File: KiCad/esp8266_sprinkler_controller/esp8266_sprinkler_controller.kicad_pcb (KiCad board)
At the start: 2 copper layers, 73.2 x 80.3 mm, 27 parts, among them J1 Barrel_Jack_Switch, J2 Screw_Terminal_01x02 ST1, J3 Screw_Terminal_01x02 ST2, J4 Screw_Terminal_01x02 ST3, J5 Screw_Terminal_01x02 ST4, SW1 SW_Push, U1 LM7805_TO220, U2 WeMos_D1_mini, U3 74HC595, U4 L293D, U5 L293D

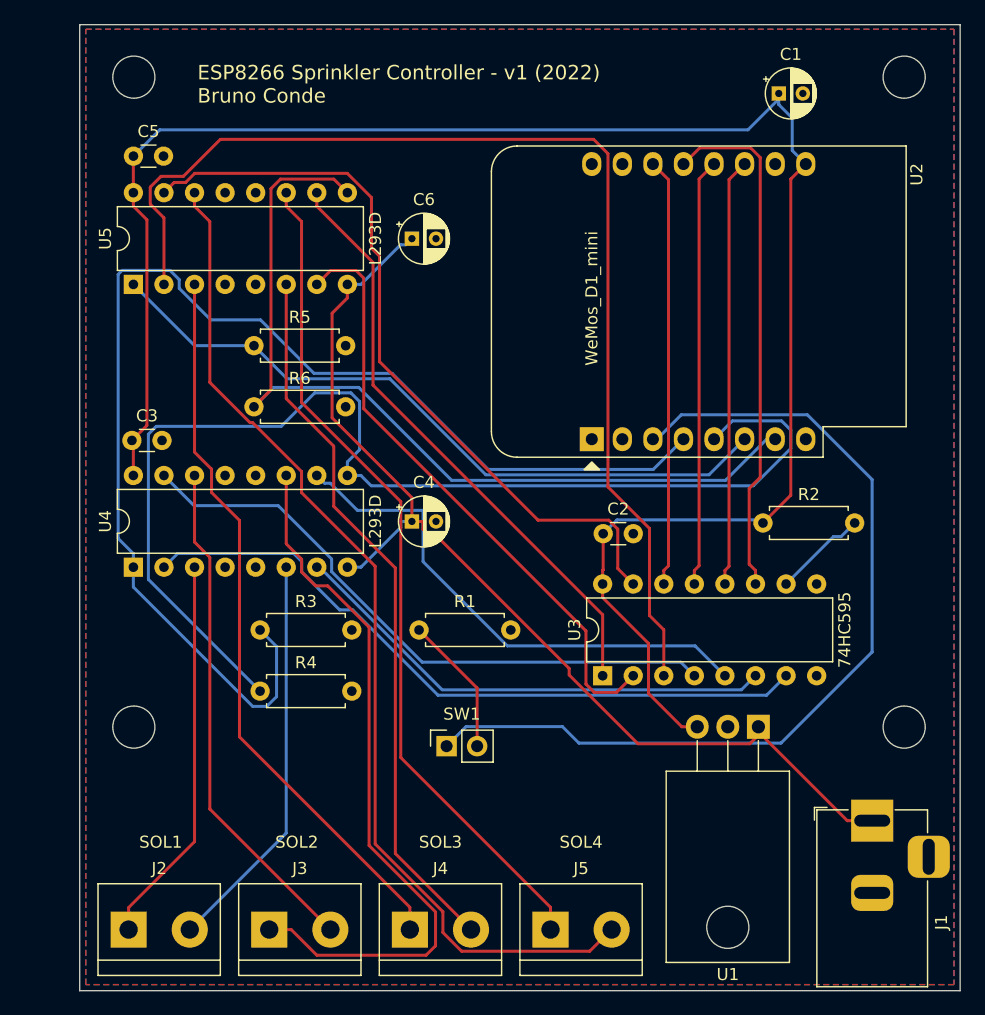
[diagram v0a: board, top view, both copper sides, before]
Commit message: Researching a way to use less power when the circuit is in deep sleep; Updated Kicad schematic and pcb design
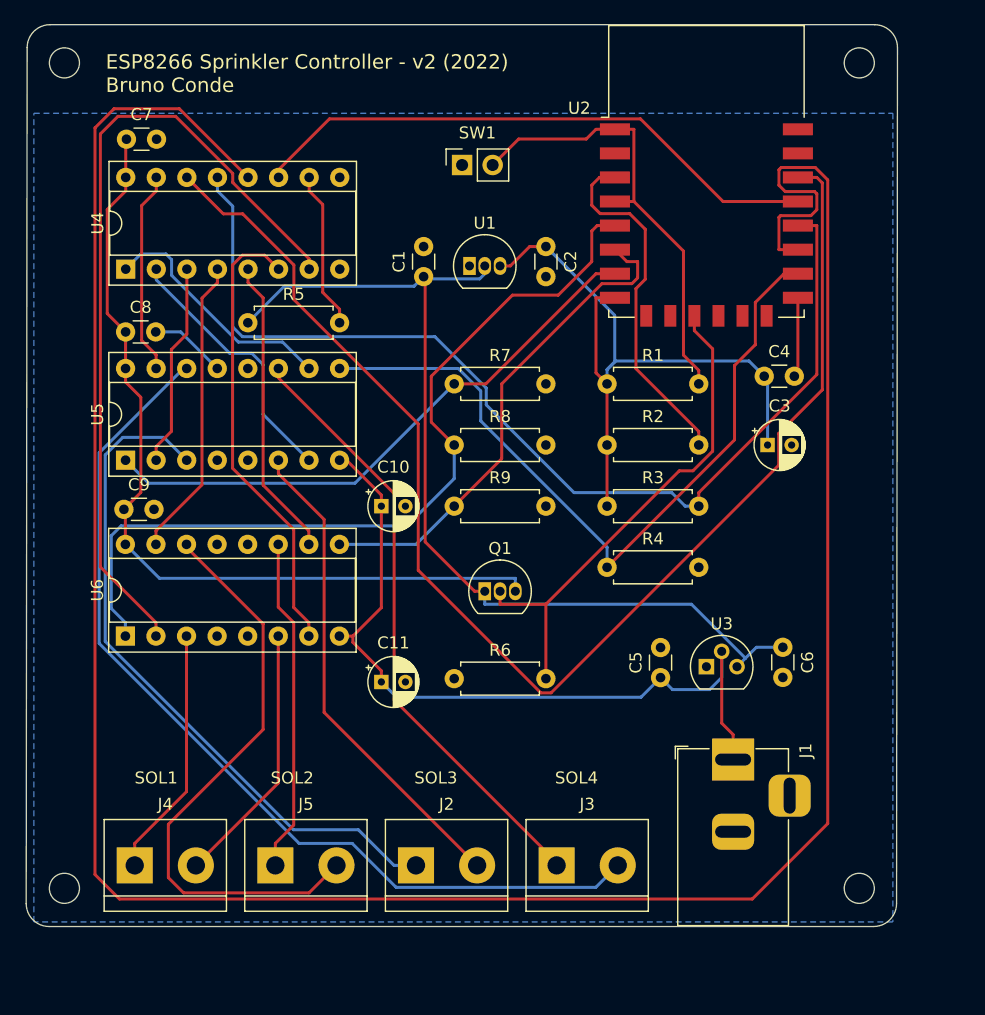
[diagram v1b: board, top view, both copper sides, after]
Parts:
- removed the R5 at (78.0, 67.3)
- removed REF** (x4): MountingHole_3.5mm, MountingHole:MountingHole_3.5mm
- added C10: C_Polarized_Small, Capacitor_THT:CP_Radial_D4.0mm_P2.00mm, F.Cu at (88.6, 80.6)
- added C2: C_Small, Capacitor_THT:C_Disc_D3.0mm_W1.6mm_P2.50mm, F.Cu at (102.2, 59.1)
- added C3: C_Polarized, Capacitor_THT:CP_Radial_D4.0mm_P2.00mm, F.Cu at (120.7, 75.6)
- added C4: C_Small, Capacitor_THT:C_Disc_D3.0mm_W1.6mm_P2.50mm, F.Cu at (120.4, 69.8)
- added C5: C_Small, Capacitor_THT:C_Disc_D3.0mm_W1.6mm_P2.50mm, F.Cu at (111.8, 94.9)
- added Q1: BC547, Package_TO_SOT_THT:TO-92_Inline, F.Cu at (97.2, 87.7)
- added R2: 10KΩ, Resistor_THT:R_Axial_DIN0207_L6.3mm_D2.5mm_P7.62mm_Horizontal, F.Cu at (107.3, 75.6)
- added R7: 1KΩ, Resistor_THT:R_Axial_DIN0207_L6.3mm_D2.5mm_P7.62mm_Horizontal, F.Cu at (94.6, 70.5)
- added R8: 1KΩ, Resistor_THT:R_Axial_DIN0207_L6.3mm_D2.5mm_P7.62mm_Horizontal, F.Cu at (94.6, 75.6)
- added R9: 1KΩ, Resistor_THT:R_Axial_DIN0207_L6.3mm_D2.5mm_P7.62mm_Horizontal, F.Cu at (94.6, 80.6)
- added REF1: MountingHole_2.5mm, MountingHole:MountingHole_2.5mm, F.Cu at (62.2, 112.4)
- added REF2: MountingHole_2.5mm, MountingHole:MountingHole_2.5mm, F.Cu at (128.3, 112.4)
- added REF3: MountingHole_2.5mm, MountingHole:MountingHole_2.5mm, F.Cu at (62.2, 43.8)
- added REF4: MountingHole_2.5mm, MountingHole:MountingHole_2.5mm, F.Cu at (128.3, 43.8)
- added U3: MCP1700-5002E_TO92, Package_TO_SOT_THT:TO-92, F.Cu at (115.6, 94.0)
- C1: value C_Polarized -> C_Small; footprint Capacitor_THT:CP_Radial_D4.0mm_P2.00mm -> Capacitor_THT:C_Disc_D3.0mm_W1.6mm_P2.50mm
- C6: value C_Polarized_Small -> C_Small; footprint Capacitor_THT:CP_Radial_D4.0mm_P2.00mm -> Capacitor_THT:C_Disc_D3.0mm_W1.6mm_P2.50mm
- R3, R4: value 1KΩ -> 10KΩ
- U1: value LM7805_TO220 -> MCP1700-3002E_TO92; footprint Package_TO_SOT_THT:TO-220-3_Horizontal_TabDown -> Package_TO_SOT_THT:TO-92_Inline
- U2: value WeMos_D1_mini -> ESP-12F; footprint Module:WEMOS_D1_mini_light -> RF_Module:ESP-12E
- U4: renamed from U3; footprint Package_DIP:DIP-16_W7.62mm -> Package_DIP:DIP-16_W7.62mm_Socket
- U5: footprint Package_DIP:DIP-16_W7.62mm -> Package_DIP:DIP-16_W7.62mm_Socket
- U6: renamed from U4; footprint Package_DIP:DIP-16_W7.62mm -> Package_DIP:DIP-16_W7.62mm_Socket
- moved U4 52.1 mm to (67.3, 61.0)
- moved C7 51.4 mm to (67.4, 50.2)
- moved SW1 48.3 mm to (95.3, 52.3)
- moved R5 45.9 mm to (77.5, 65.4)
- moved C6 45.9 mm to (121.9, 92.4), turned to -90 degrees
- moved U1 45.2 mm to (95.9, 60.7), turned to 0 degrees
- moved C1 33.2 mm to (92.1, 61.6), turned to 90 degrees
- moved R3 30.6 mm to (107.3, 80.6)
- moved R4 30.6 mm to (107.3, 85.7)
- moved R6 28.1 mm to (94.6, 95.0)
- moved R1 25.7 mm to (107.3, 70.5)
- moved U2 24.2 mm to (115.6, 52.8), turned to 0 degrees
- moved C8 14.6 mm to (67.3, 66.2)
- moved U5 14.6 mm to (67.3, 76.8)
- moved C11 13.6 mm to (88.6, 95.2)
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- renumbered C4 to C11, C2 to C7, C5 to C8, C3 to C9, J4 to J2, J5 to J3, J2 to J4, J3 to J5, R2 to R5
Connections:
- net Net-(U3-Pad1) renamed /QB
- net Net-(U3-Pad15) renamed /QA
- net Net-(U3-Pad2) renamed /QC
- net Net-(U3-Pad3) renamed /QD
- net Net-(U3-Pad4) renamed /QE
- net Net-(U3-Pad5) renamed /QF
- net Net-(U3-Pad6) renamed /QG
- net Net-(U3-Pad7) renamed /QH
- C6 pad 1: +9V -> +5V
- C7 pad 1: +5V -> /+5V_EN
- C8 pad 1: +5V -> /+5V_EN
- C9 pad 1: +5V -> /+5V_EN
- R1 pad 1: Net-(R1-Pad1) -> +3V3
- R1 pad 2: GND -> Net-(R1-Pad2)
- R3 pad 1: Net-(R3-Pad1) -> +3V3
- R3 pad 2: GND -> /GPIO0
- R4 pad 1: Net-(R4-Pad1) -> /GPIO15
- R6 pad 1: Net-(R6-Pad1) -> GND
- R6 pad 2: GND -> /GPIO9
- SW1 pad 1: Net-(SW1-Pad1) -> GND
- SW1 pad 2: Net-(R1-Pad1) -> Net-(R1-Pad2)
- U1 pad 1: +9V -> GND
- U1 pad 2: GND -> +5V
- U1 pad 3: +5V -> +3V3
- U2 pad 1: unconnected-(U2-Pad1) -> Net-(R1-Pad2)
- U2 pad 10: GND -> unconnected-(U2-Pad10)
- U2 pad 11: Net-(U2-Pad11) -> /GPIO9
- U2 pad 12: Net-(U2-Pad12) -> unconnected-(U2-Pad12)
- U2 pad 13: Net-(U2-Pad13) -> unconnected-(U2-Pad13)
- U2 pad 14: Net-(U2-Pad14) -> unconnected-(U2-Pad14)
- U2 pad 15: unconnected-(U2-Pad15) -> GND
- U2 pad 16: unconnected-(U2-Pad16) -> /GPIO15
- U2 pad 3: Net-(SW1-Pad1) -> Net-(R2-Pad2)
- U2 pad 4: Net-(R3-Pad1) -> Net-(R1-Pad2)
- U2 pad 5: Net-(R4-Pad1) -> /GPIO14
- U2 pad 6: Net-(R5-Pad1) -> /GPIO12
- U2 pad 7: Net-(R6-Pad1) -> /GPIO13
- U2 pad 8: unconnected-(U2-Pad8) -> +3V3
- U2 pad 9: +5V -> unconnected-(U2-Pad9)
- U4 pad 11: Net-(U2-Pad13) -> /GPIO4
- U4 pad 12: Net-(U2-Pad11) -> /GPIO2
- U4 pad 13: Net-(U2-Pad12) -> /GPIO0
- U4 pad 14: Net-(U2-Pad14) -> /GPIO5
- U4 pad 16: +5V -> /+5V_EN
- U5 pad 1: Net-(R5-Pad1) -> /GPIO13
- U5 pad 16: +5V -> /+5V_EN
- U5 pad 9: Net-(R6-Pad1) -> /GPIO15
- U6 pad 1: Net-(R3-Pad1) -> /GPIO14
- U6 pad 16: +5V -> /+5V_EN
- U6 pad 9: Net-(R4-Pad1) -> /GPIO12
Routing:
- net /GPIO2: track 0.00 -> 213.9 mm
- net /GPIO5: track 0.00 -> 110.7 mm
- net Net-(R3-Pad1): track 104.4 -> 0.00 mm
- net Net-(R4-Pad1): track 98.3 -> 0.00 mm
- net /GPIO0: track 0.00 -> 87.6 mm
- net /QD: track 94.0 -> 16.9 mm
- net Net-(SW1-Pad1): track 75.0 -> 0.00 mm
- net Net-(R6-Pad1): track 74.4 -> 0.00 mm
- net +5V: track 154.2 -> 80.0 mm
- net /+5V_EN: track 0.00 -> 70.8 mm
- net /GPIO14: track 0.00 -> 70.5 mm
- net /GPIO15: track 0.00 -> 63.1 mm
- net Net-(R5-Pad1): track 58.6 -> 0.00 mm
- net +3V3: track 0.00 -> 57.5 mm
- net /GPIO13: track 0.00 -> 48.7 mm
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- removed copper zone on F.Cu, net GND
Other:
- board size 73.2 x 80.3 mm -> 72.4 x 74.9 mm
- board text added: "ESP8266 Sprinkler Controller - v2 (2022) Bruno Conde"
- board text removed: "ESP8266 Sprinkler Controller - v1 (2022) Bruno Conde"

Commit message: Refactor esp8266 code; New Kicad schematic version (v2.0) to make the circuit battery efficient
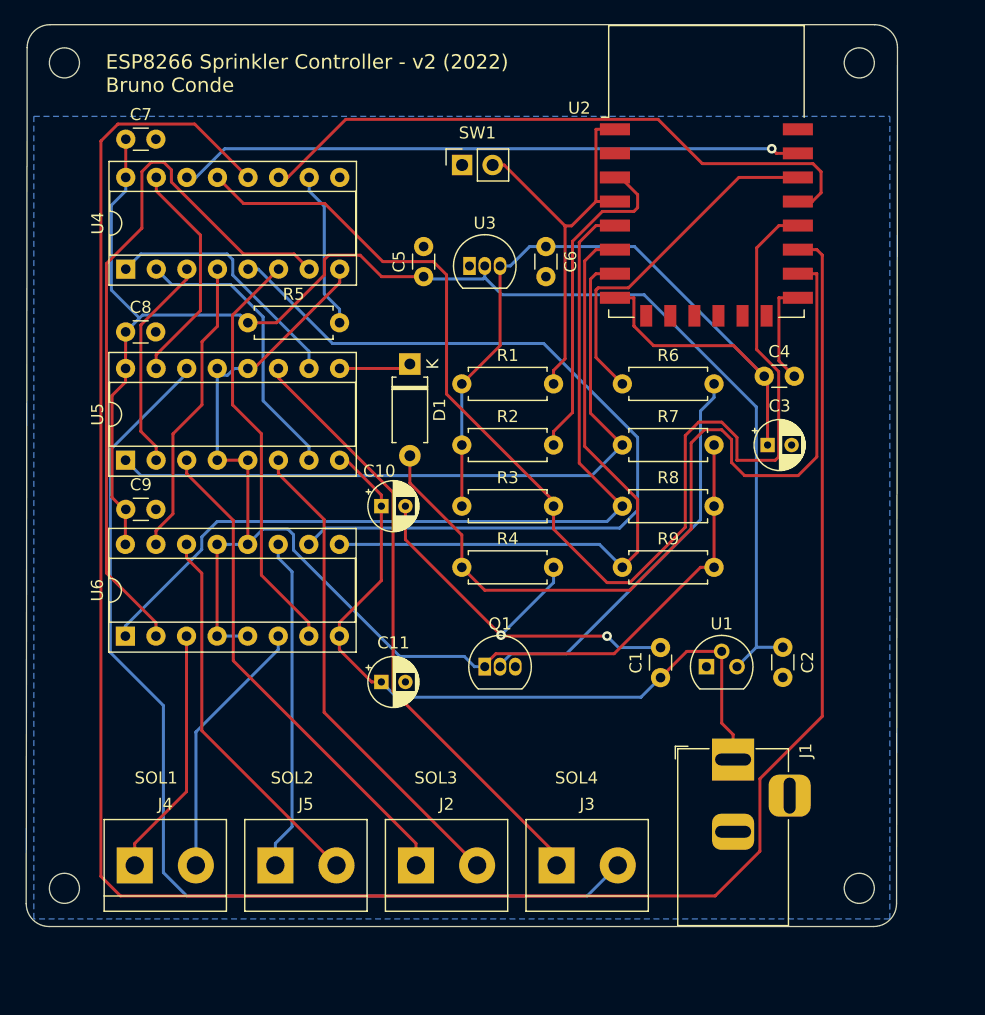
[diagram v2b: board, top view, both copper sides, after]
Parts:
- added D1: D_Schottky, Diode_THT:D_A-405_P7.62mm_Horizontal, F.Cu at (90.9, 68.8)
- R6: value 1KΩ -> 10KΩ
- moved R6 28.2 mm to (108.6, 70.5)
- moved R7 14.9 mm to (108.6, 75.6)
- moved R8 14.9 mm to (108.6, 80.6)
- moved R9 14.9 mm to (108.6, 85.7)
- moved R1 12.1 mm to (95.2, 70.5)
- moved R2 12.1 mm to (95.2, 75.6)
- moved R3 12.1 mm to (95.2, 80.6)
- moved R4 12.1 mm to (95.2, 85.7)
- moved Q1 6.27 mm to (97.2, 94.0)
- moved C9 0.16 mm to (67.3, 80.9)
- moved C7 0.06 mm to (67.3, 50.2)
- renumbered C5 to C1, C6 to C2, C1 to C5, C2 to C6, U3 to U1, U1 to U3
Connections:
- C7 pad 1: /+5V_EN -> +5V
- C8 pad 1: /+5V_EN -> +5V
- C9 pad 1: /+5V_EN -> +5V
- Q1 pad 1: +5V -> /GND_EN
- Q1 pad 2: /GPIO9 -> Net-(Q1-Pad2)
- Q1 pad 3: /+5V_EN -> GND
- R6 pad 1: GND -> /GPIO5
- R6 pad 2: /GPIO9 -> Net-(Q1-Pad2)
- R7 pad 2: GND -> /GND_EN
- R8 pad 2: GND -> /GND_EN
- R9 pad 2: GND -> /GND_EN
- U2 pad 11: /GPIO9 -> unconnected-(U2-Pad11)
- U2 pad 21: unconnected-(U2-Pad21) -> /GPIO3
- U4 pad 14: /GPIO5 -> /GPIO3
- U4 pad 16: /+5V_EN -> +5V
- U4 pad 8: GND -> /GND_EN
- U5 pad 12: GND -> /GND_EN
- U5 pad 13: GND -> /GND_EN
- U5 pad 16: /+5V_EN -> +5V
- U5 pad 4: GND -> /GND_EN
- U5 pad 5: GND -> /GND_EN
- U5 pad 9: /GPIO15 -> Net-(D1-Pad1)
- U6 pad 12: GND -> /GND_EN
- U6 pad 13: GND -> /GND_EN
- U6 pad 16: /+5V_EN -> +5V
- U6 pad 4: GND -> /GND_EN
- U6 pad 5: GND -> /GND_EN
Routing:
- net /GND_EN: track 0.00 -> 102.8 mm
- net /GPIO5: track 110.7 -> 29.4 mm
- net /+5V_EN: track 70.8 -> 0.00 mm
- net /GPIO3: track 0.00 -> 51.9 mm, vias 0 -> 1
- net /QF: track 25.0 -> 72.7 mm
- net /GPIO9: track 42.1 -> 0.00 mm
- net +5V: track 80.0 -> 121.9 mm
- net Net-(Q1-Pad2): track 0.00 -> 33.6 mm
- net GND: track 13.7 -> 43.8 mm, vias 0 -> 2
- net /GPIO2: track 213.9 -> 186.6 mm
- net Net-(J5-Pad2): track 49.0 -> 31.8 mm
- net Net-(J2-Pad1): track 57.2 -> 41.6 mm
- net /GPIO0: track 87.6 -> 102.6 mm
- net /GPIO12: track 41.2 -> 55.0 mm
- net +3V3: track 57.5 -> 70.7 mm
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
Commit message: KiCad: Revision 3 of schematic abdnd PCB. Solved a couple of circuit problems:  - Added a Schottky Diode between the reset line and GPIO16    so this pin is not shorted when the reset button is pressed.  - Added a Schottky Diode between GPIO15 and the enable pin of the L293D
ESP8266: Force a loop call to the MQTT broker when interface_mode is not active
as MQTT messages were not being published correctly because the ESP8266 would
go into deep sleep before it finished processing the messages.
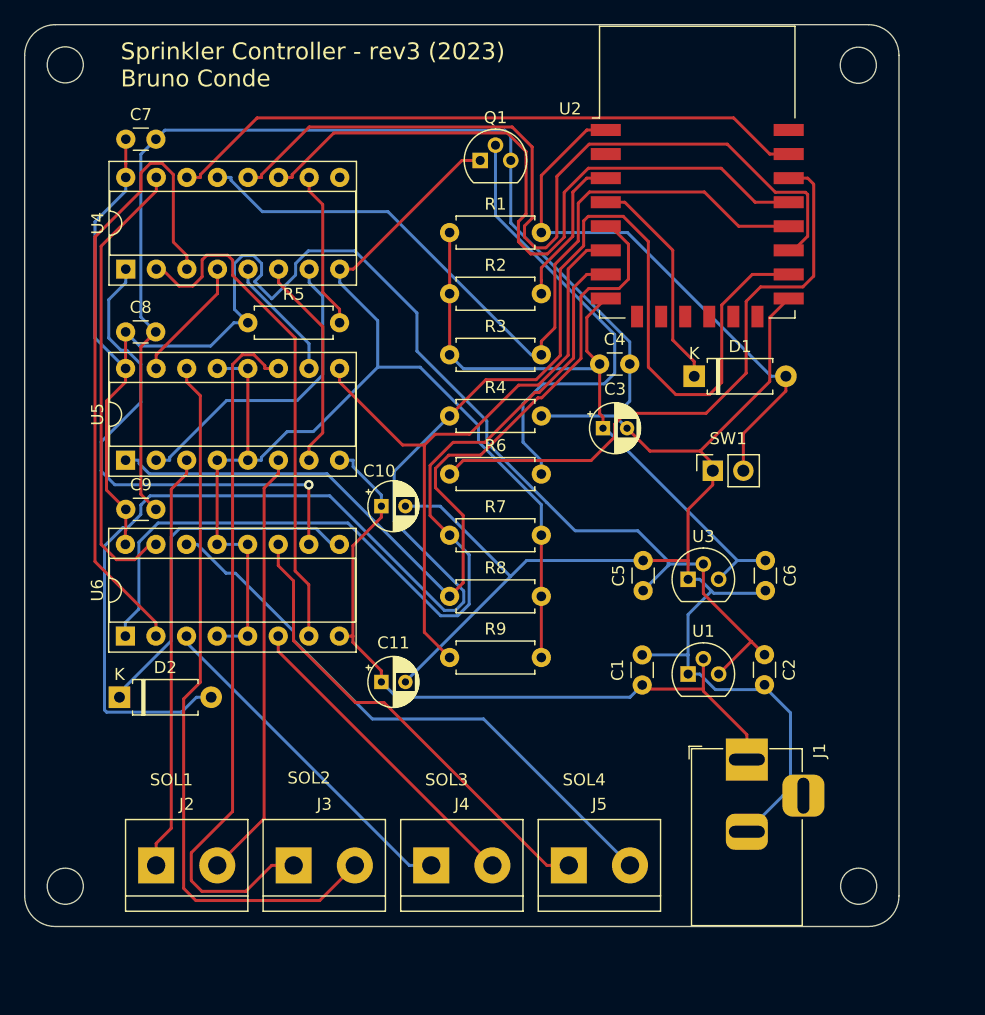
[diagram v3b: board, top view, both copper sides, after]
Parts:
- removed REF1, REF2, REF3, REF4: MountingHole_2.5mm, MountingHole:MountingHole_2.5mm
- added D2: D_Schottky, Diode_THT:D_A-405_P7.62mm_Horizontal, F.Cu at (66.8, 96.5)
- added Hole1: MountingHole_3mm, MountingHole:MountingHole_3mm, F.Cu at (62.3, 44.0)
- added Hole2: MountingHole_3mm, MountingHole:MountingHole_3mm, F.Cu at (128.2, 44.0)
- added Hole3: MountingHole_3mm, MountingHole:MountingHole_3mm, F.Cu at (62.3, 112.2)
- added Hole4: MountingHole_3mm, MountingHole:MountingHole_3mm, F.Cu at (128.2, 112.2)
- J2: value Screw_Terminal_01x02 ST3 -> Screw_Terminal_01x02 ST1
- J3: value Screw_Terminal_01x02 ST4 -> Screw_Terminal_01x02 ST2
- J4: value Screw_Terminal_01x02 ST1 -> Screw_Terminal_01x02 ST3
- J5: value Screw_Terminal_01x02 ST2 -> Screw_Terminal_01x02 ST4
- Q1: value BC547 -> SS8050CBU; footprint Package_TO_SOT_THT:TO-92_Inline -> Package_TO_SOT_THT:TO-92
- R6: value 10KΩ -> 100Ω
- U3: footprint Package_TO_SOT_THT:TO-92_Inline -> Package_TO_SOT_THT:TO-92
- moved Q1 42.1 mm to (96.8, 51.9)
- moved SW1 32.8 mm to (116.1, 77.7)
- moved C5 31.8 mm to (110.3, 87.7)
- moved C6 31.8 mm to (120.5, 85.2)
- moved U3 31.7 mm to (114.0, 86.7)
- moved J4 24.6 mm to (92.7, 110.5)
- moved J5 24.4 mm to (104.1, 110.5)
- moved D1 23.6 mm to (114.6, 69.8), turned to 0 degrees
- moved J3 21.8 mm to (81.3, 110.5)
- moved J2 21.6 mm to (69.8, 110.5)
- moved R7 16.2 mm to (94.2, 83.1)
- moved R8 16.2 mm to (94.2, 88.1)
- moved R9 16.2 mm to (94.2, 93.2)
- moved R6 16.2 mm to (94.2, 78.0)
- moved C3 13.7 mm to (107.0, 74.2)
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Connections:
- D1 pad 2: /GPIO15 -> Net-(D1-Pad2)
- R1 pad 2: Net-(R1-Pad2) -> Net-(D1-Pad2)
- SW1 pad 2: Net-(R1-Pad2) -> Net-(D1-Pad2)
- U2 pad 1: Net-(R1-Pad2) -> Net-(D1-Pad2)
- U2 pad 4: Net-(R1-Pad2) -> Net-(D1-Pad1)
- U5 pad 1: /GPIO13 -> /GPIO14
- U5 pad 10: /QB -> /QF
- U5 pad 15: /QA -> /QE
- U5 pad 2: /QD -> /QH
- U5 pad 7: /QC -> /QG
- U5 pad 9: Net-(D1-Pad1) -> /GPIO12
- U6 pad 1: /GPIO14 -> /GPIO13
- U6 pad 10: /QF -> /QB
- U6 pad 15: /QE -> /QA
- U6 pad 2: /QH -> /QD
- U6 pad 7: /QG -> /QC
- U6 pad 9: /GPIO12 -> Net-(D2-Pad1)
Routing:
- net GND: track 43.8 -> 213.4 mm, vias 2 -> 0
- net /GPIO2: track 186.6 -> 71.6 mm
- net /GPIO15: track 71.2 -> 139.7 mm
- net /QF: track 72.7 -> 10.4 mm
- net Net-(D1-Pad2): track 0.00 -> 46.2 mm
- net /GPIO0: track 102.6 -> 66.1 mm
- net /QD: track 18.0 -> 53.9 mm
- net Net-(R1-Pad2): track 34.2 -> 0.00 mm
- net /QH: track 60.0 -> 26.2 mm
- net Net-(D2-Pad1): track 0.00 -> 29.9 mm
- net Net-(J3-Pad2): track 85.9 -> 60.1 mm
- net /GPIO5: track 29.4 -> 51.1 mm
- net /QB: track 21.3 -> 42.8 mm, vias 0 -> 1
- net /QA: track 18.9 -> 38.0 mm
- net /QC: track 24.0 -> 42.8 mm
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- removed copper zone on B.Cu, net GND
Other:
- board size 72.4 x 74.9 mm -> 72.6 x 74.9 mm
- board text added: "Sprinkler Controller - rev3 (2023) Bruno Conde"
- board text removed: "ESP8266 Sprinkler Controller - v2 (2022) Bruno Conde"
